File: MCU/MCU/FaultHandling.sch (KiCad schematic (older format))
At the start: 35 parts, among them Q6 8550, Q7 8050, Q8 8550, Q9 8050

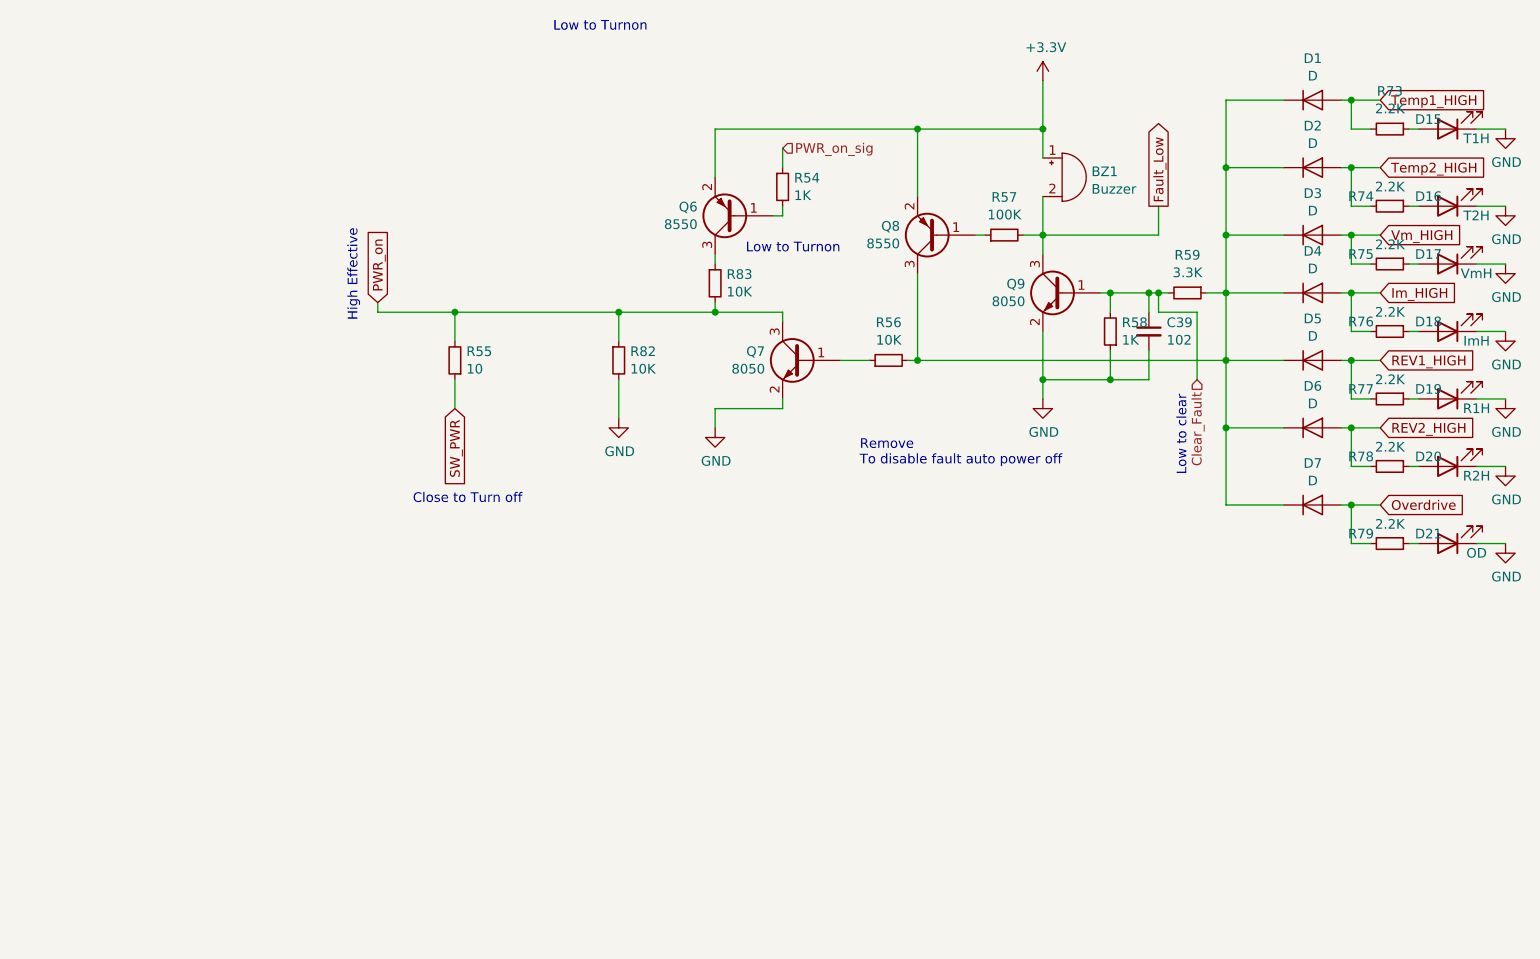
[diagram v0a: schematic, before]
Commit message: OPA1000 and 2000 compatibility
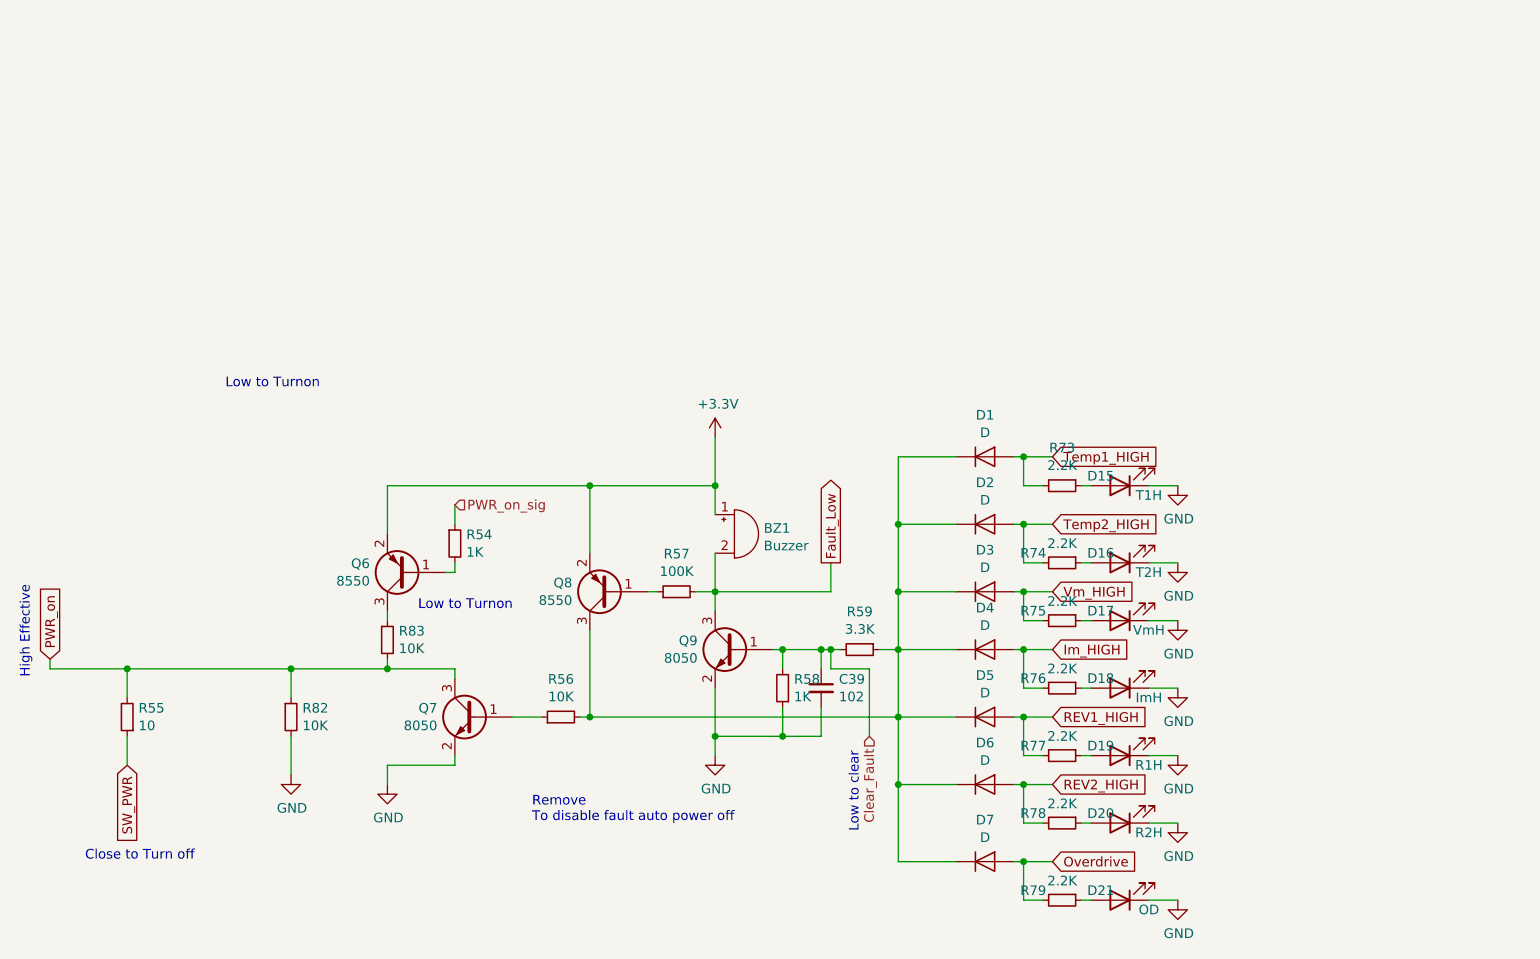
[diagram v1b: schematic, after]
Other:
- moved on the sheet: BZ1, C39, D1, D15, D16, D17, D18, D19, D2, D20, D21, D3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
